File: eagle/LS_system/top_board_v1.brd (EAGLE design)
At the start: 47 x 31.8 mm, 18 parts, among them IC1 74HC595D, X1 MURDOCK_STACK

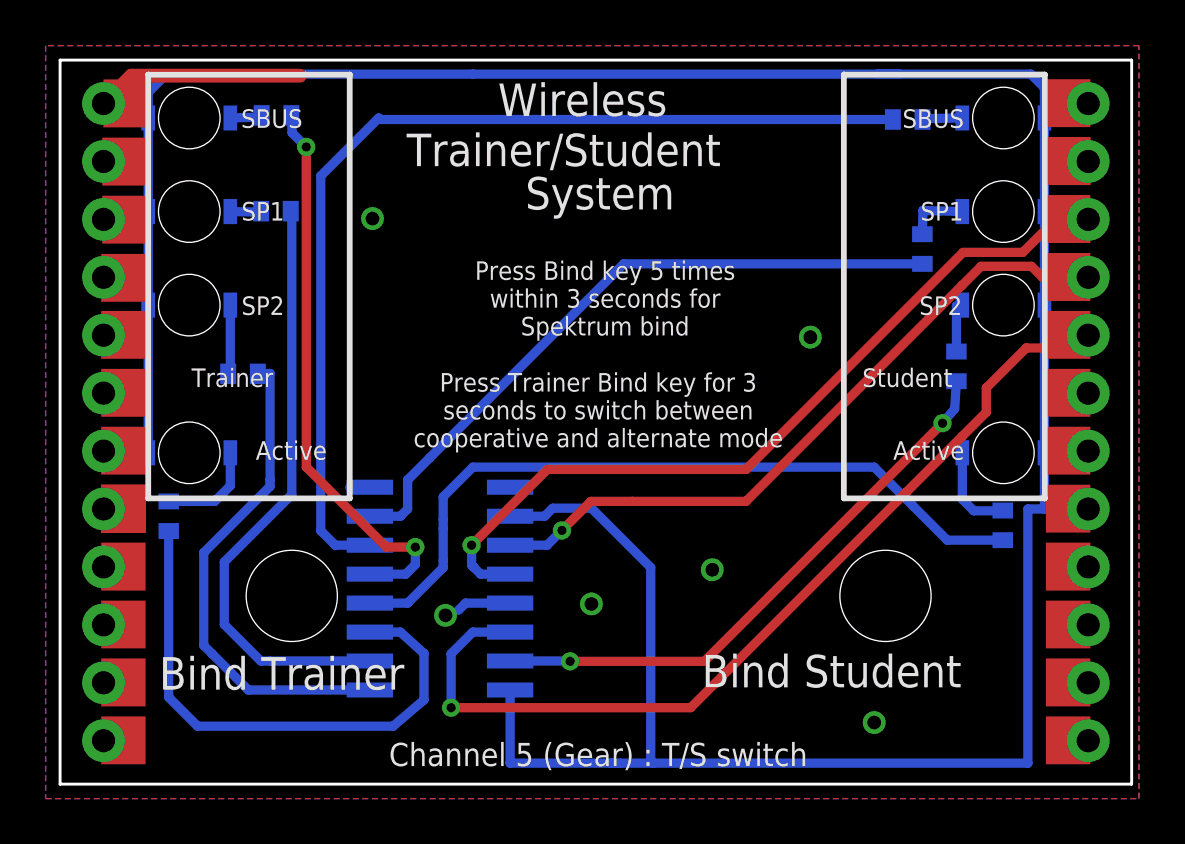
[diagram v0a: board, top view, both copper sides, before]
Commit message: mirrored spektrum & moved buttons
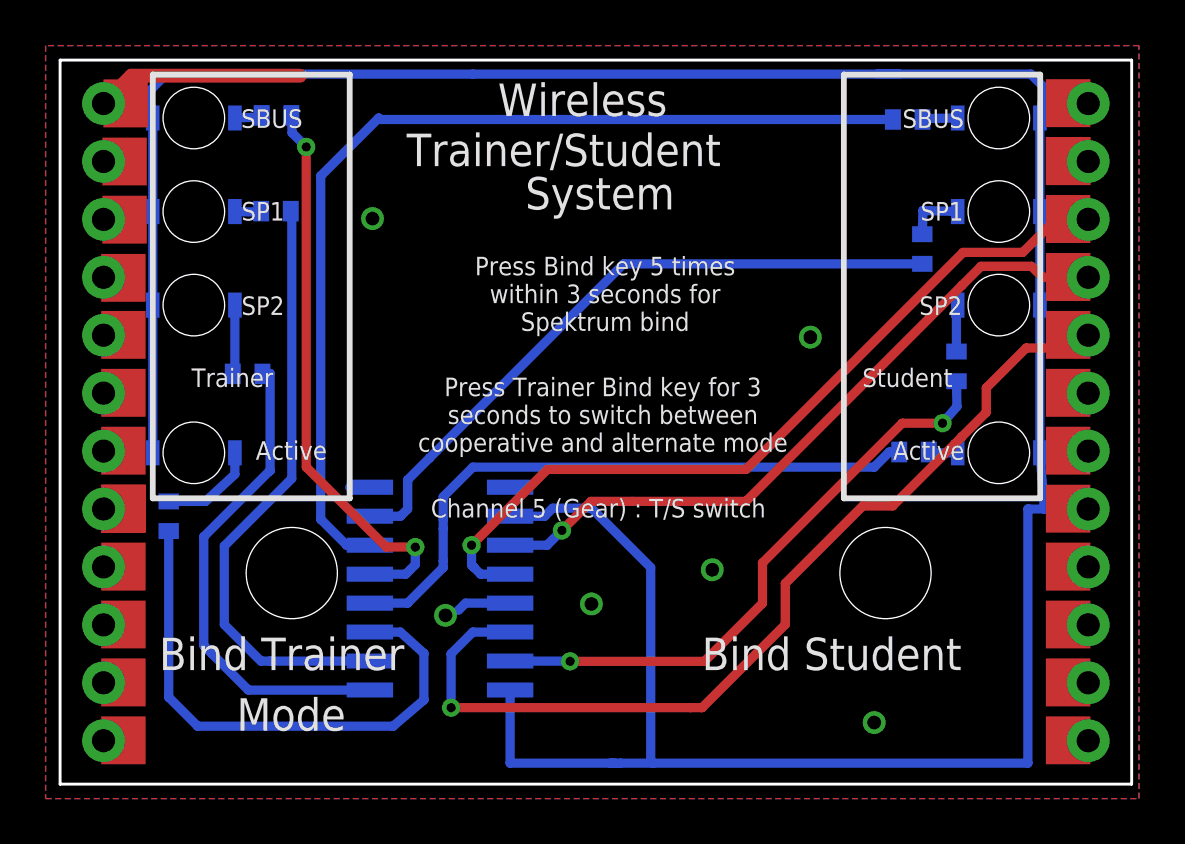
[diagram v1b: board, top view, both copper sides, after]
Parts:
- moved R6 5.05 mm to (37.4, 14.6), turned to 180 degrees
- moved LED1 0.20 mm to (41.2, 21.0)
- moved LED14 0.20 mm to (41.2, 14.5)
- moved LED15 0.20 mm to (41.2, 29.2)
- moved LED16 0.20 mm to (41.2, 25.1)
- moved LED2 0.20 mm to (5.87, 21.0)
- moved LED3 0.20 mm to (5.87, 25.1)
- moved LED4 0.20 mm to (5.87, 14.5)
- moved LED6 0.20 mm to (5.87, 29.2)
- moved R15 0.20 mm to (8.22, 18.0)
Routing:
- net QE: track 33.4 -> 27.8 mm
- net N$7: track 4.03 -> 1.28 mm
- net QA: track 25.3 -> 26.4 mm
- net LED_D: track 40.7 -> 41.7 mm
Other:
- board text added: "Mode"

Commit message: conneced LEDs to switche 3v3
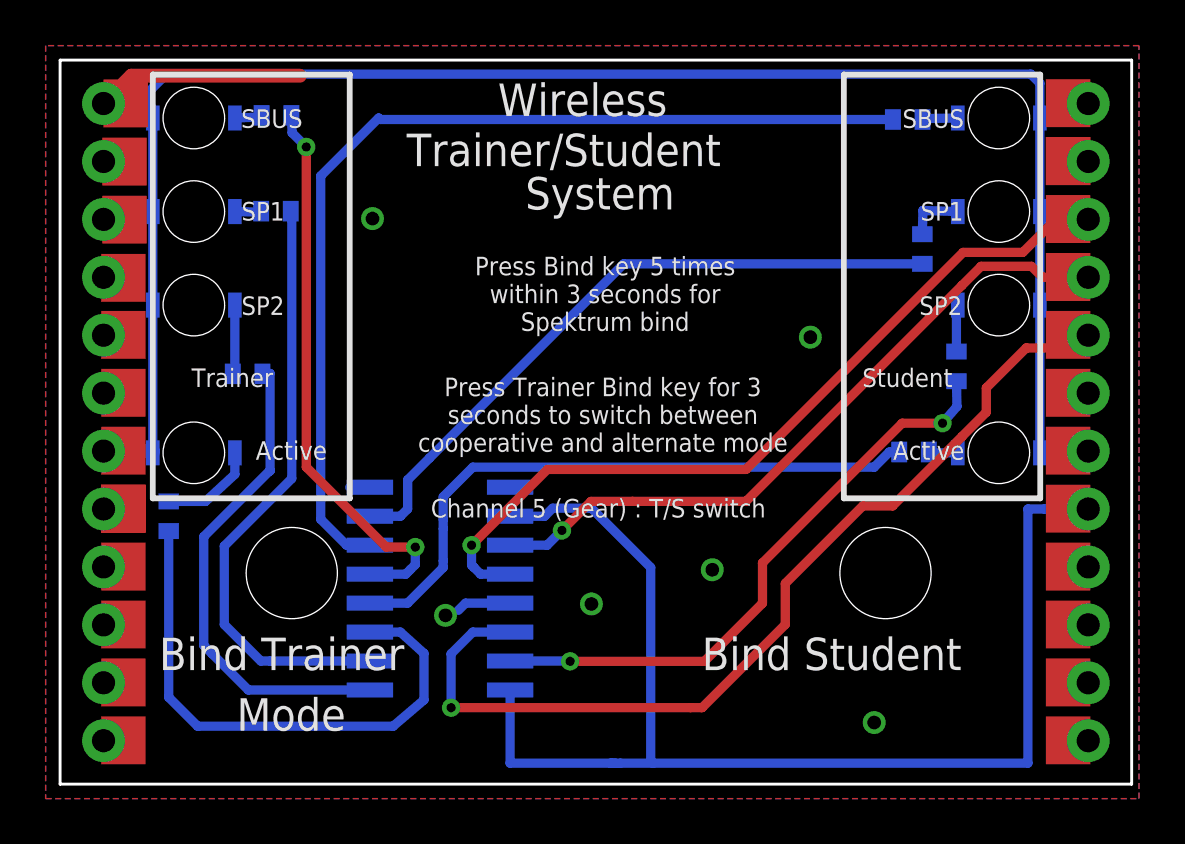
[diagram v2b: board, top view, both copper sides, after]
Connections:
- new net 3V3_SP: LED1.A, LED14.A, LED15.A, LED16.A, LED2.A, LED3.A, LED4.A, LED6.A, X1.3V3_SP
- net 3.3V: no longer LED1.A, LED14.A, LED15.A, LED16.A, LED2.A, LED3.A, LED4.A, LED6.A
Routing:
- net 3.3V: track 131.1 -> 55.9 mm
- net 3V3_SP: track 0.00 -> 73.9 mm
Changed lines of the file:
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@@
 <?xml version="1.0" encoding="utf-8"?>
 <!DOCTYPE eagle SYSTEM "eagle.dtd">
-<eagle version="6.4">
+<eagle version="6.3">
 <drawing>
 <settings>
@@
 <grid distance="0.1" unitdist="mm" unit="mm" style="lines" multiple="1" display="no" altdistance="0.025" altunitdist="inch" altunit="inch"/>
 <layers>
-<layer number="1" name="Top" color="4" fill="1" visible="yes" active="yes"/>
+<layer number="1" name="Top" color="4" fill="1" visible="no" active="yes"/>
 <layer number="2" name="Route2" color="1" fill="3" visible="no" active="no"/>
 <layer number="3" name="Route3" color="4" fill="3" visible="no" active="no"/>
@@
 <layer number="14" name="Route14" color="1" fill="6" visible="no" active="no"/>
 <layer number="15" name="Route15" color="4" fill="6" visible="no" active="no"/>
-<layer number="16" name="Bottom" color="1" fill="1" visible="no" active="yes"/>
+<layer number="16" name="Bottom" color="1" fill="1" visible="yes" active="yes"/>
 <layer number="17" name="Pads" color="2" fill="1" visible="yes" active="yes"/>
 <layer number="18" name="Vias" color="2" fill="1" visible="yes" active="yes"/>
@@
 <signal name="3.3V">
 <contactref element="IC1" pad="10"/>
-<contactref element="LED1" pad="A"/>
-<contactref element="LED2" pad="A"/>
-<contactref element="LED3" pad="A"/>
-<contactref element="LED4" pad="A"/>
-<contactref element="LED6" pad="A"/>
-<contactref element="LED16" pad="A"/>
-<contactref element="LED15" pad="A"/>
-<contactref element="LED14" pad="A"/>
 <contactref element="IC1" pad="16"/>
 <wire x1="42.44" y1="12.065" x2="43.165" y2="12.065" width="0.4064" layer="16"/>
@@
 <wire x1="24.565" y1="0.92" x2="26" y2="0.92" width="0.4064" layer="16"/>
 <wire x1="26" y1="0.92" x2="42.44" y2="0.92" width="0.4064" layer="16"/>
-<wire x1="4.665" y1="31.135" x2="18.1080875" y2="31.135" width="0.4064" layer="16"/>
-<wire x1="35.815" y1="31.135" x2="36.8" y2="31.135" width="0.4064" layer="16"/>
-<wire x1="36.8" y1="31.135" x2="42.565" y2="31.135" width="0.4064" layer="16"/>
-<wire x1="42.565" y1="31.135" x2="43.165" y2="30.535" width="0.4064" layer="16"/>
-<wire x1="43.165" y1="30.535" x2="42.965" y2="29.21" width="0.4064" layer="16"/>
-<wire x1="42.965" y1="29.21" x2="42.965" y2="25.1079" width="0.4064" layer="16"/>
-<wire x1="42.965" y1="25.1079" x2="42.965" y2="21.0058" width="0.4064" layer="16"/>
-<wire x1="42.965" y1="21.0058" x2="42.965" y2="14.5288" width="0.4064" layer="16"/>
-<wire x1="42.965" y1="14.5288" x2="43.165" y2="12.065" width="0.4064" layer="16"/>
-<wire x1="4.065" y1="14.5288" x2="4.065" y2="21.0058" width="0.4064" layer="16"/>
-<wire x1="4.065" y1="21.0058" x2="4.065" y2="25.1079" width="0.4064" layer="16"/>
-<wire x1="4.065" y1="29.21" x2="4.065" y2="25.1079" width="0.4064" layer="16"/>
-<wire x1="3.865" y1="30.335" x2="4.065" y2="29.21" width="0.4064" layer="16"/>
 <contactref element="X1" pad="3V3"/>
-<wire x1="3.865" y1="30.335" x2="4.665" y2="31.135" width="0.4064" layer="16"/>
 <wire x1="24.565" y1="0.92" x2="24.15" y2="0.92" width="0.4064" layer="16"/>
 <wire x1="24.15" y1="0.92" x2="19.7334" y2="0.92" width="0.4064" layer="16"/>
 <wire x1="19.7334" y1="0.92" x2="19.7334" y2="4.1275" width="0.4064" layer="16"/>
 <wire x1="24.365" y1="0.92" x2="24.15" y2="0.92" width="0.4064" layer="16"/>
-<wire x1="18.1080875" y1="31.135" x2="36.8" y2="31.135" width="0.4064" layer="16"/>
 <wire x1="19.7334" y1="11.7475" x2="21.2475" y2="11.7475" width="0.4064" layer="16"/>
 <wire x1="21.2475" y1="11.7475" x2="21.6" y2="12.1" width="0.4064" layer="16"/>
@@
 <wire x1="36.365" y1="14.565" x2="36.7975" y2="14.565" width="0.4064" layer="16"/>
 </signal>
+<signal name="3V3_SP">
+<contactref element="X1" pad="3V3_SP"/>
+<contactref element="LED16" pad="A"/>
+<contactref element="LED15" pad="A"/>
+<contactref element="LED14" pad="A"/>
+<wire x1="42.965" y1="29.21" x2="42.965" y2="25.1079" width="0.4064" layer="16"/>
+<contactref element="LED1" pad="A"/>
+<contactref element="LED2" pad="A"/>
+<contactref element="LED3" pad="A"/>
+<contactref element="LED4" pad="A"/>
+<contactref element="LED6" pad="A"/>
+<wire x1="4.065" y1="14.5288" x2="4.065" y2="21.0058" width="0.4064" layer="16"/>
+<wire x1="4.065" y1="21.0058" x2="4.065" y2="25.1079" width="0.4064" layer="16"/>
+<wire x1="4.065" y1="29.21" x2="4.065" y2="25.1079" width="0.4064" layer="16"/>
+<wire x1="3.865" y1="30.335" x2="4.065" y2="29.21" width="0.4064" layer="16"/>
+<wire x1="3.865" y1="30.335" x2="4.665" y2="31.135" width="0.4064" layer="16"/>
+<wire x1="4.665" y1="31.135" x2="42.565" y2="31.135" width="0.4064" layer="16"/>
+<wire x1="1.905" y1="14.605" x2="4.065" y2="14.605" width="0.6096" layer="16"/>
+<wire x1="4.065" y1="14.605" x2="4.065" y2="14.5288" width="0.6096" layer="16"/>
+<wire x1="42.565" y1="31.135" x2="42.965" y2="30.735" width="0.4064" layer="16"/>
+<wire x1="42.965" y1="30.735" x2="42.965" y2="29.21" width="0.4064" layer="16"/>
+<wire x1="42.965" y1="25.1079" x2="42.965" y2="21.0058" width="0.4064" layer="16"/>
+<wire x1="42.965" y1="21.0058" x2="42.965" y2="14.5288" width="0.4064" layer="16"/>
+</signal>
 </signals>
